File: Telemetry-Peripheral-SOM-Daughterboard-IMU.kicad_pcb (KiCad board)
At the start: 2 copper layers, 24 x 50 mm, 6 parts, among them J1 Conn_02x10_Odd_Even, U1 LSM6DSV

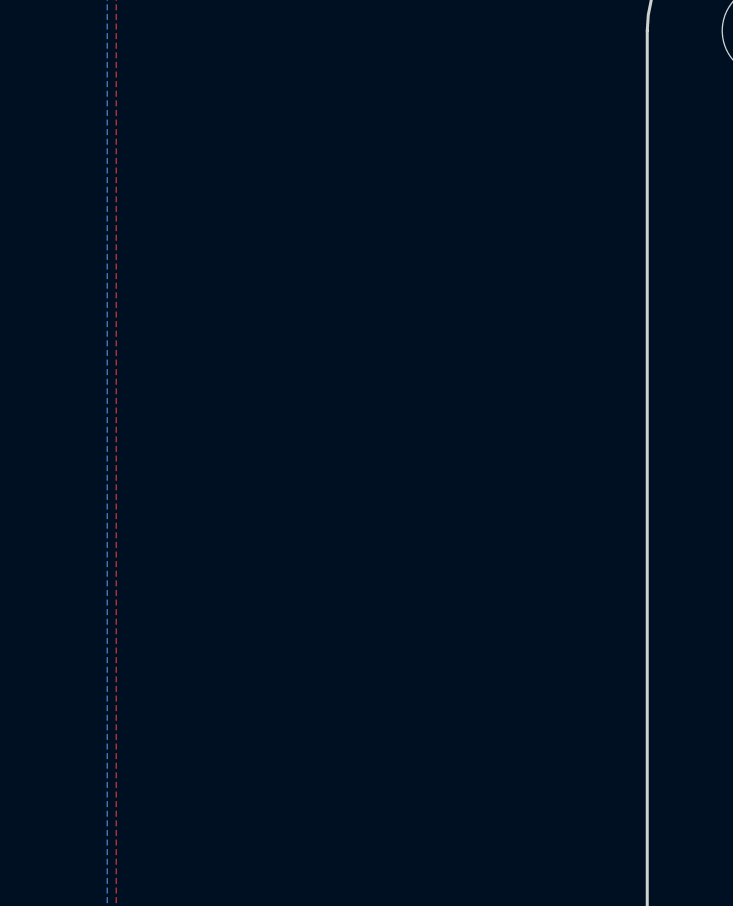
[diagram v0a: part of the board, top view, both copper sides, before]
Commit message: temp sensor library fix
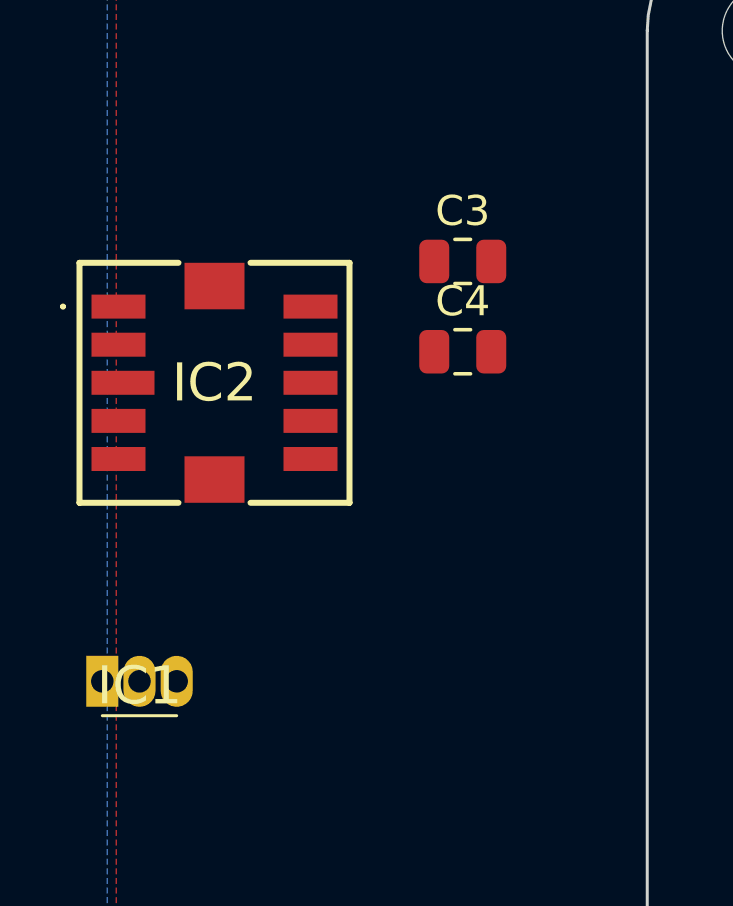
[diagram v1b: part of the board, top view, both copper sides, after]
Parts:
- added C3: 0.1u, Capacitor_SMD:C_0805_2012Metric, F.Cu at (139.8, 77.7)
- added C4: 0.1u, Capacitor_SMD:C_0805_2012Metric, F.Cu at (139.8, 80.7)
- added IC1: LMT87LPG, UTSVT_ICs:LMT87LPG, F.Cu at (127.8, 91.7)
- added IC2: FS3000-1015, UTSVT_Special:FS30001015, F.Cu at (131.6, 81.7)

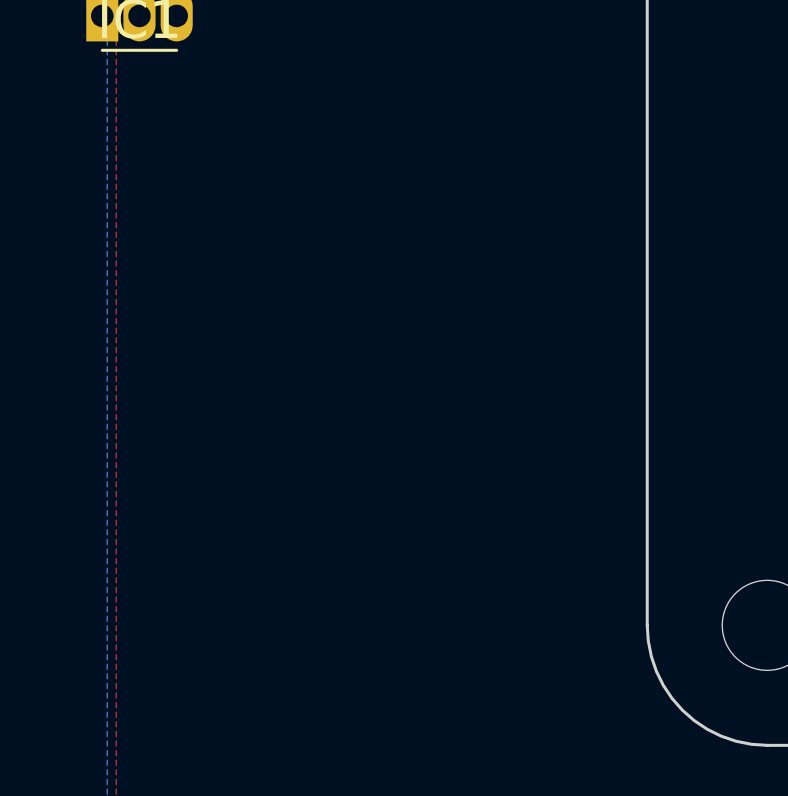
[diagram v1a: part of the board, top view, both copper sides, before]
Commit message: assigned footprints for all capacitors
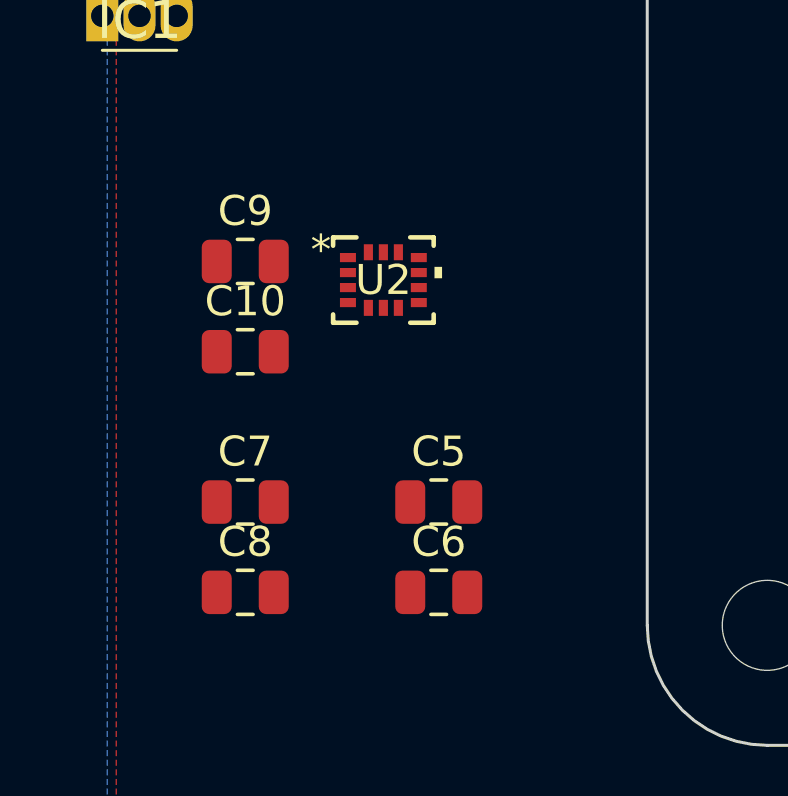
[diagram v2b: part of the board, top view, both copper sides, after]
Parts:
- added C10: 0.1u, Capacitor_SMD:C_0805_2012Metric, F.Cu at (132.6, 102.9)
- added C5: 0.1u, Capacitor_SMD:C_0805_2012Metric, F.Cu at (139.1, 107.9)
- added C6: 1u, Capacitor_SMD:C_0805_2012Metric, F.Cu at (139.1, 110.9)
- added C7: 0.1u, Capacitor_SMD:C_0805_2012Metric, F.Cu at (132.6, 107.9)
- added C8: 0.1u, Capacitor_SMD:C_0805_2012Metric, F.Cu at (132.6, 110.9)
- added C9: 0.1u, Capacitor_SMD:C_0805_2012Metric, F.Cu at (132.6, 99.9)
- added U2: LSM6DSV, UTSVT_Special:LGA14-L_2P59X3P1X0P5_STM, F.Cu at (137.2, 100.5)
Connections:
- IC1 pad 1: Net-(IC1-OUT) -> /SPI1_NSS

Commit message: first draft
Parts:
- removed IC2: FS3000-1015, UTSVT_Special:FS30001015
- removed U2: LSM6DSV, UTSVT_Special:LGA14-L_2P59X3P1X0P5_STM
- added C11: 10n, Capacitor_SMD:C_0805_2012Metric, F.Cu at (161.7, 111.0)
- added C12: 0.1u, Capacitor_SMD:C_0805_2012Metric, F.Cu at (157.9, 111.0)
- added J2: Conn_01x03_Pin, UTSVT_Connectors:Molex_MicroFit3.0_1x3xP3.00mm_PolarizingPeg_Vertical, B.Cu at (163.1, 68.7)
- added J3: Conn_01x03_Pin, UTSVT_Connectors:Molex_MicroFit3.0_1x3xP3.00mm_PolarizingPeg_Vertical, B.Cu at (148.9, 78.3)
- added J4: Conn_01x03_Pin, UTSVT_Connectors:Molex_MicroFit3.0_1x3xP3.00mm_PolarizingPeg_Vertical, B.Cu at (157.2, 113.3)
- added R1: 50, Resistor_SMD:R_0805_2012Metric, F.Cu at (167.5, 83.4)
- C1, C2: moved to F.Cu
- C10: moved to B.Cu
- C7: value 0.1u -> 10n
- C9: value 0.1u -> 10n; moved to B.Cu
- IC1: value LMT87LPG -> FS3000-1015; footprint UTSVT_ICs:LMT87LPG -> UTSVT_Special:FS30001015; moved to B.Cu
- U1: footprint UTSVT_ICs:LGA14-L_2P59X3P1X0P5_STM -> UTSVT_Special:LGA14-L_2P59X3P1X0P5_STM
- moved C8 49.7 mm to (161.9, 70.8), turned to 180 degrees
- moved C7 45.0 mm to (158.1, 70.8)
- moved C10 37.7 mm to (164.4, 82.7), turned to -90 degrees
- moved C9 33.9 mm to (161.8, 82.6), turned to -90 degrees
- moved IC1 23.7 mm to (151.4, 94.4), turned to -90 degrees
- moved C2 20.5 mm to (163.4, 78.5)
- moved C6 17.1 mm to (148.0, 96.3), turned to -90 degrees
- moved C1 16.9 mm to (158.4, 82.6), turned to -90 degrees
- moved U1 16.4 mm to (163.1, 82.7)
- moved C3 16.2 mm to (150.3, 90.1)
- moved C4 15.6 mm to (150.3, 92.3)
- moved C5 14.9 mm to (150.8, 98.8), turned to 180 degrees
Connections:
- C4 pad 1: Net-(IC2-VREG) -> Net-(IC1-VREG)
- C5 pad 1: Net-(IC2-TP1) -> Net-(IC1-TP1)
- C5 pad 2: Net-(IC2-TP2) -> Net-(IC1-TP2)
- C6 pad 1: Net-(IC2-VCM) -> Net-(IC1-VCM)
- C9 pad 1: +3.3V -> /ADC1_IN
- IC1 pad 1: /SPI1_NSS -> Net-(IC1-VREG)
- IC1 pad 2: GND -> +3.3V
- IC1 pad 3: +3.3V -> GND
- J1 pad 2: +3.3V -> /ADC1_IN
- J1 pad 4: GND -> /ADC2_IN
- U1 pad 1: /SPI1_MISO -> Net-(U1-SDO/SA0)
- U1 pad 12: /SPI1_NSS -> /SPI2_NSS
- U1 pad 13: /SPI1_SCK -> /SPI2_SCK
- U1 pad 14: /SPI1_MOSI -> /SPI2_MOSI
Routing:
- net /I2C2_SDA: track 20.5 -> 0.15 mm
- net /SPI2_MISO: track 0.00 -> 19.3 mm
- net /SPI1_SCK: track 7.87 -> 0.00 mm
- net /SPI1_MISO: track 6.72 -> 0.00 mm
- net Net-(U1-SDO/SA0): track 0.00 -> 6.65 mm
- net /SPI1_MOSI: track 5.39 -> 0.00 mm
- net +3.3V: track 11.6 -> 6.53 mm
- net GND: track 6.33 -> 11.1 mm, vias 3 -> 2
- net /SPI1_NSS: track 3.64 -> 0.00 mm, vias 2 -> 0
- net /I2C2_SCL: track 12.5 -> 10.4 mm
- net /ADC2_IN: vias 0 -> 1
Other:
- board text added: "Telemetry Peripheral SOM Daughterboard IMU Fall 2023 - Design by Andrew Nguyen, Frank Li, Jim Fang"
- board text removed: "Telemetry Peripheral SOM Daughterboard IMU Fall 2023 - Design by Andrew Nguyen"

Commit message: a
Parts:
- C10, C9, J2, J3, J4: moved to F.Cu
- U1: moved to B.Cu
- moved J2 37.5 mm to (159.0, 106.0), turned to 0 degrees
- moved C8 29.6 mm to (157.0, 100.0)
- moved C7 27.2 mm to (157.0, 98.0), turned to 180 degrees
- moved J3 18.6 mm to (165.0, 69.0), turned to 180 degrees
- moved C11 15.9 mm to (152.5, 98.0)
- moved C12 12.3 mm to (152.5, 100.0), turned to 180 degrees
- moved C5 8.64 mm to (155.5, 91.5), turned to 0 degrees
- moved C6 7.84 mm to (155.5, 94.0), turned to 180 degrees
- moved C1 7.64 mm to (164.5, 78.0), turned to 180 degrees
- moved C10 6.80 mm to (161.0, 76.8)
- moved C9 6.52 mm to (159.0, 76.8)
- moved U1 4.96 mm to (165.0, 78.1)
- moved R1 4.53 mm to (164.5, 80.0)
- moved IC1 4.00 mm to (153.5, 91.0), turned to 0 degrees
- moved C2 2.78 mm to (164.5, 76.0), turned to 0 degrees
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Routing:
- net /ADC2_IN: track 0.00 -> 48.6 mm, vias 1 -> 2
- net /ADC1_IN: track 0.00 -> 29.4 mm, vias 0 -> 2
- net /SPI1_NSS: track 0.00 -> 19.0 mm
- net /I2C2_SDA: track 0.15 -> 17.3 mm, vias 2 -> 1
- net /I2C1_SDA: track 0.00 -> 13.8 mm, vias 0 -> 1
- net /I2C1_SCL: track 0.00 -> 13.8 mm, vias 0 -> 1
- net /SPI2_NSS: track 0.00 -> 12.8 mm, vias 0 -> 1
- net /SPI2_SCK: track 0.00 -> 11.6 mm, vias 0 -> 1
- net GND: track 11.1 -> 1.64 mm, vias 2 -> 12
- net /SPI2_MISO: track 19.3 -> 10.4 mm
- net /SPI2_MOSI: track 0.00 -> 8.59 mm, vias 0 -> 1
- net Net-(U1-SDO/SA0): track 6.65 -> 0.00 mm
- net Net-(IC1-VREG): track 0.00 -> 4.47 mm, vias 0 -> 1
- net /I2C2_SCL: track 10.4 -> 14.4 mm, vias 2 -> 1
- net Net-(IC1-VCM): track 0.00 -> 3.73 mm, vias 0 -> 1
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- added copper zone on B.Cu, net +3.3V
- added copper zone on F.Cu, net GND
